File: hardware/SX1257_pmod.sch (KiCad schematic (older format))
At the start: 5 parts, among them J1 Conn_02x06_Odd_Even, U1 SX1257, Y1 32/36MHz ?ppm

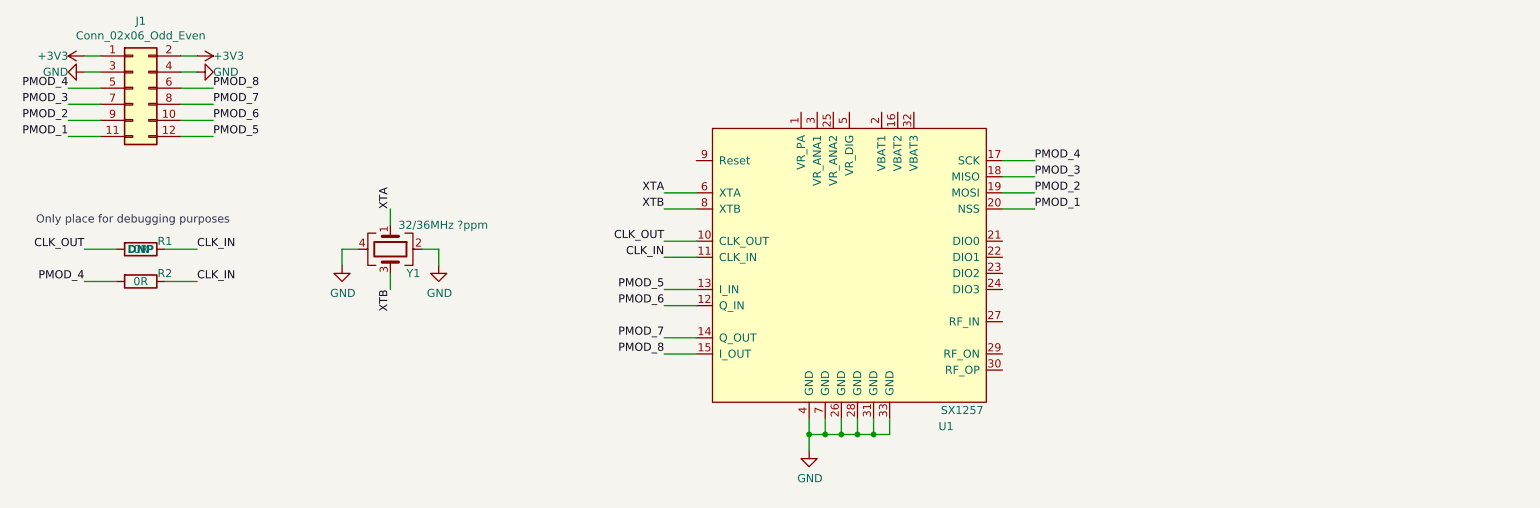
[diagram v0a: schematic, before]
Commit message: Added some caps etc
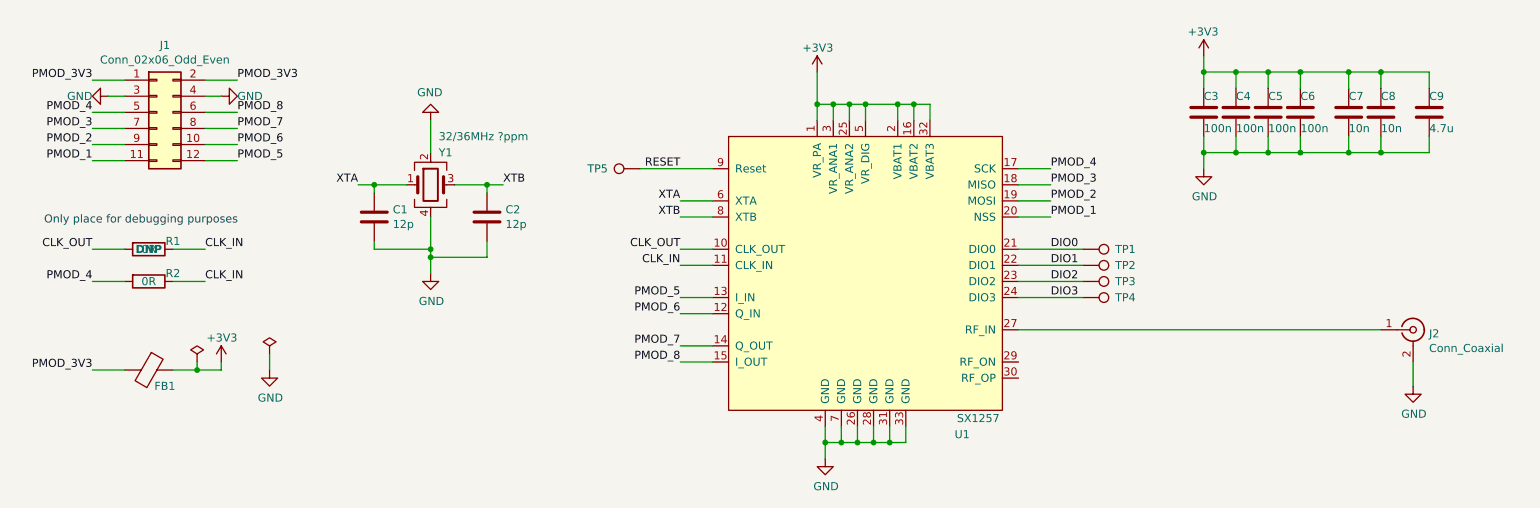
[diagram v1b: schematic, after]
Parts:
- added C1, C2: 12p, symbol Device:C
- added C3, C4, C5, C6: 100n, symbol Device:C
- added C7, C8: 10n, symbol Device:C
- added C9: 4.7u, symbol Device:C
- added FB1: Ferrite_Bead, symbol Device:Ferrite_Bead
- added J2: Conn_Coaxial, symbol Connector:Conn_Coaxial
- added TP1, TP2, TP3, TP4, TP5: TestPoint, symbol Connector:TestPoint
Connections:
- net +3V3: now also U1.1 (VR_PA), U1.16 (VBAT2), U1.2 (VBAT1), U1.25 (VR_ANA2), U1.3 (VR_ANA1), U1.32 (VBAT3), U1.5 (VR_DIG), C3.1, C4.1, C5.1, C6.1, C7.1, C8.1, C9.1, FB1.1; no longer J1.1 (Pin_1), J1.2 (Pin_2)
- net GND: now also C1.2, C2.2, C3.2, C4.2, C5.2, C6.2, C7.2, C8.2, C9.2, J2.2 (Ext)
- net XTA: now also C1.1
- net XTB: now also C2.1
- net DIO0: now reaches U1.21 (DIO0)
- net DIO0: now also TP1.1
- net DIO1: now reaches U1.22 (DIO1)
- net DIO1: now also TP2.1
- net DIO2: now reaches U1.23 (DIO2)
- net DIO2: now also TP3.1
- net DIO3: now reaches U1.24 (DIO3)
- net DIO3: now also TP4.1
- net at U1.27 (RF_IN): now also J2.1 (In)
- net RESET: now reaches U1.9 (Reset)
- net RESET: now also TP5.1
- new net PMOD_3V3: FB1.2, J1.1 (Pin_1), J1.2 (Pin_2)
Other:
- moved on the sheet: J1, R1, R2, U1, Y1

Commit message: Finalized the schematic
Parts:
- added AE1, AE2: PCB_Ant, symbol Device:Antenna
- added C10: 2.7p, symbol Device:C
- added C11, C12: 33p, symbol Device:C
- added C13, C16: 10p, symbol Device:C
- added C14: 3.3p, symbol Device:C
- added C15: 5.6p, symbol Device:C
- added C17, C18: 1u, symbol Device:C
- added C19: 10u, symbol Device:C
- added J3: SMA_F_TX, symbol Connector:Conn_Coaxial
- added L1: 15nH, symbol Device:L
- added L2: 10n, symbol Device:L
- added L3: 12n, symbol Device:L
- added R3, R4, R5, R6: 0R, symbol Device:R
- C1, C2: value 12p -> 16p
- C9: value 4.7u -> 1u
- J2: value Conn_Coaxial -> SMA_F_RX
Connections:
- net +3V3: now also C17.1, C18.1, C19.1
- net GND: now also C10.2, C12.2, C14.2, C15.2, C17.2, C18.2, C19.2, J3.2 (Ext), L3.2
- net at J2.1 (In): now also R4.1; no longer U1.27 (RF_IN)
- net RF_ON: now reaches U1.29 (RF_ON)
- net RF_ON: now also C11.2, C12.1
- net RF_OP: now reaches U1.30 (RF_OP)
- net RF_OP: now also C11.1, L2.1
- new net: C13.1, C15.1, L3.1, R3.2, R4.2
- new net: C13.2, L1.2
- new net: J3.1 (In), R6.1
- new net: C16.1, R5.2, R6.2
- new net: C14.1, C16.2, L2.2
- new net: AE2.1 (A), R5.1
- new net: AE1.1 (A), R3.1
- new net RF_IN: C10.1, L1.1, U1.27 (RF_IN)
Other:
- note added: "Check if 10mH or 10nH!"
- note added: "Not connected through the PMOD.\nRegisters are available through SPI."
- moved on the sheet: C1, C2, C3, C4, C5, C6, C7, C8, C9, TP1, TP2, TP3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

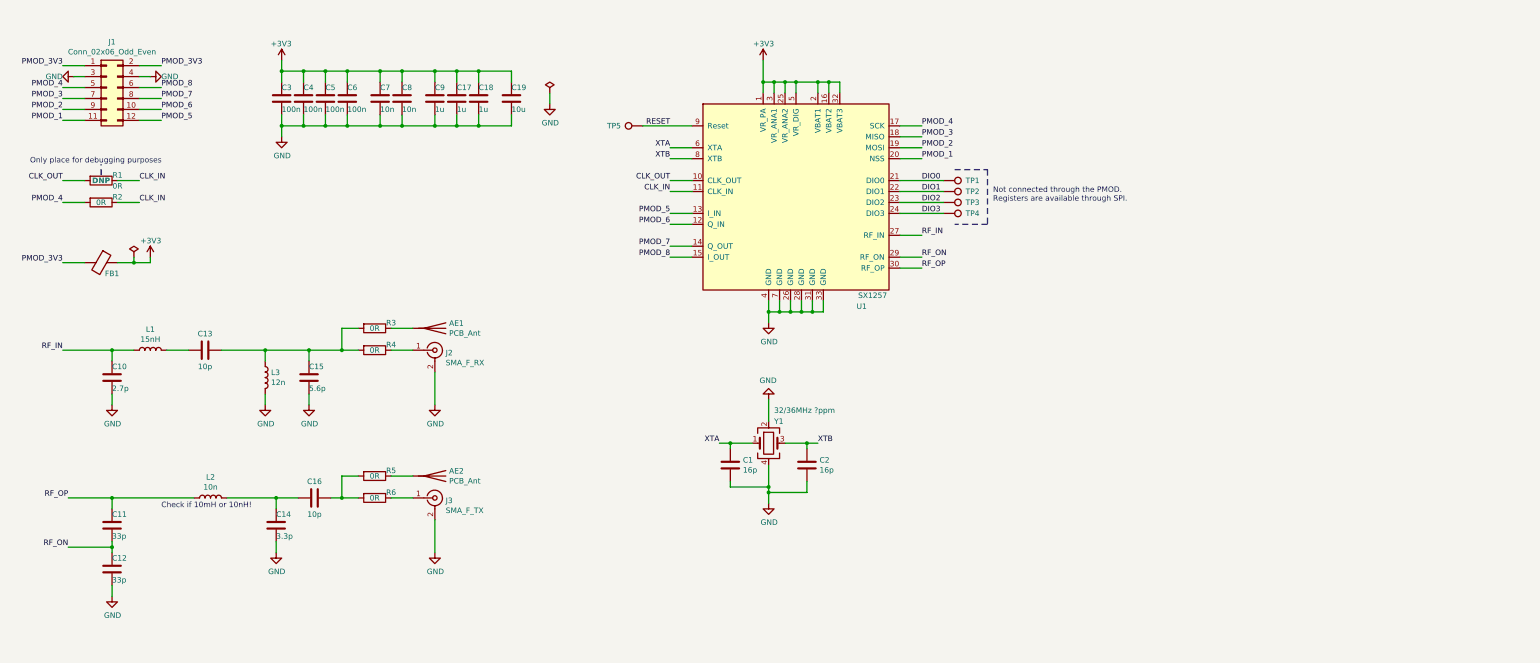
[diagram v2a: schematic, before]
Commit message: Remove CLK_OUT 0R and tidy up a bit.
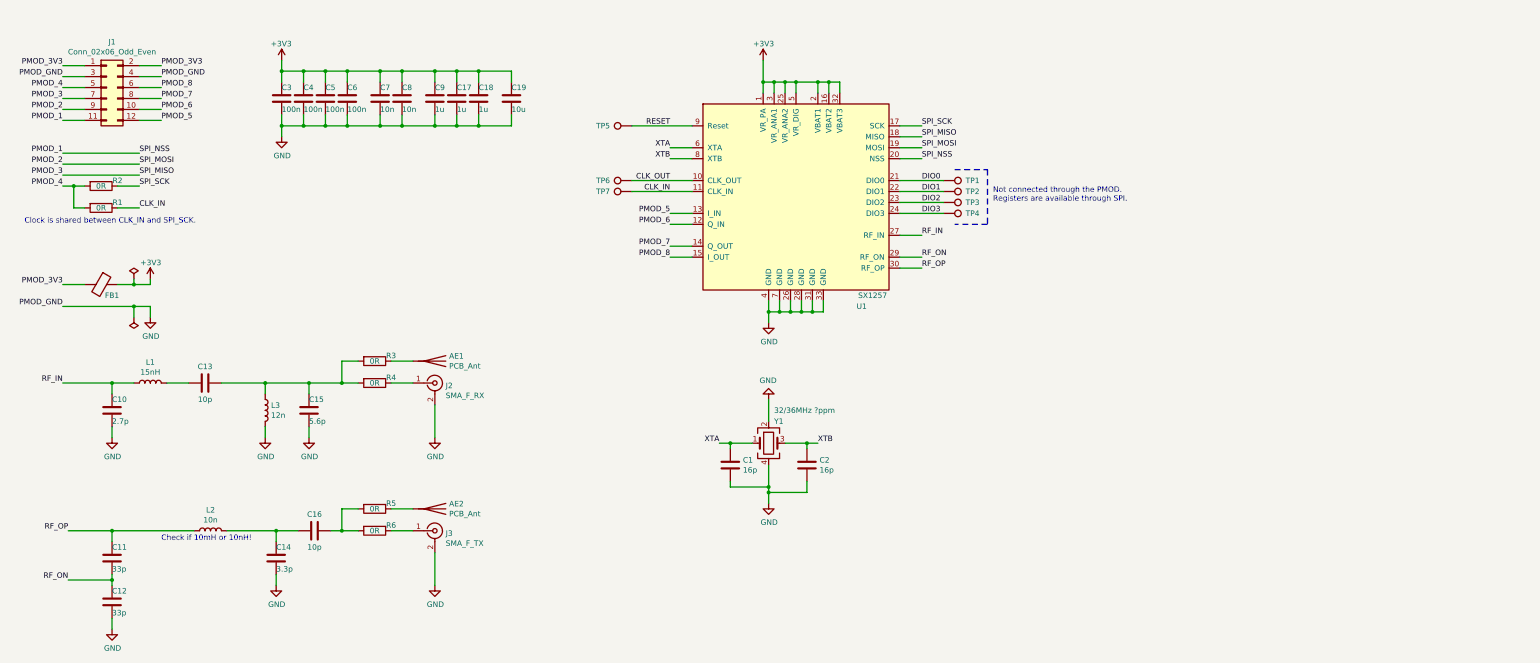
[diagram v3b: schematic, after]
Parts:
- added TP6, TP7: TestPoint, symbol Connector:TestPoint
- R1: Placement DNP -> (none)
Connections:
- net CLK_IN: now also TP7.1; no longer R2.1
- net CLK_OUT: now also TP6.1; no longer R1.2
- net PMOD_4: now also R1.2; no longer U1.17 (SCK)
- new net SPI_SCK: R2.1, U1.17 (SCK)
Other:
- note added: "Clock is shared between CLK_IN and SPI_SCK."
- note removed: "Only place for debugging purposes"
- moved on the sheet: AE1, AE2, C10, C11, C12, C13, C14, C15, C16, FB1, J2, J3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

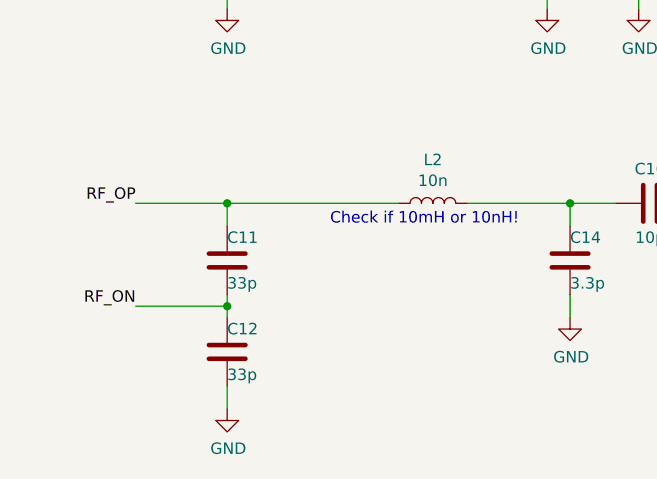
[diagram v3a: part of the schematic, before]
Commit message: Fix incorrect value of C11 33p => 3.3p
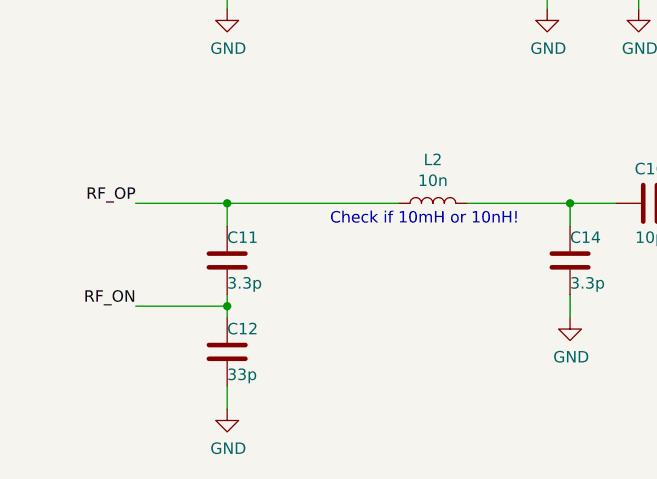
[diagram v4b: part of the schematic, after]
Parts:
- C11: value 33p -> 3.3p
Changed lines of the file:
@@
 P 1450 5550
 F 0 "C11" H 1450 5650 50  0000 L CNN
-F 1 "33p" H 1450 5450 50  0000 L CNN
+F 1 "3.3p" H 1450 5450 50  0000 L CNN
 F 2 "" H 1488 5400 50  0001 C CNN
 F 3 "~" H 1450 5550 50  0001 C CNN

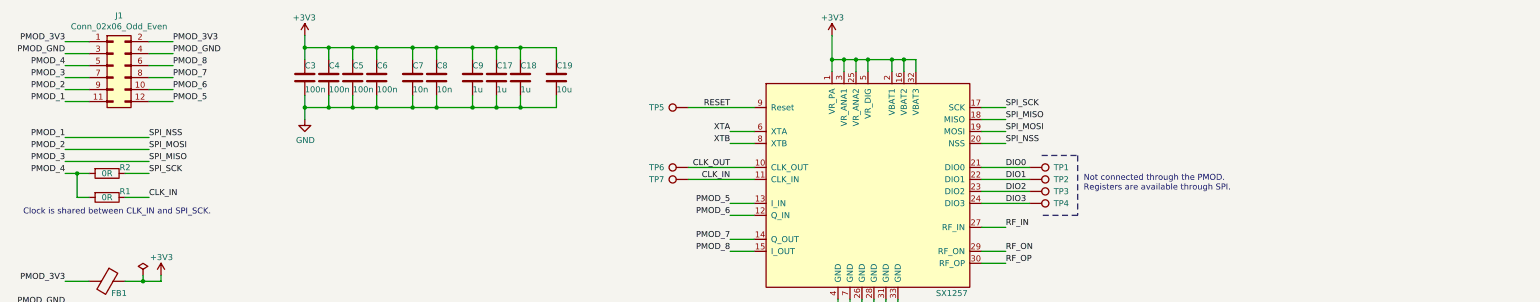
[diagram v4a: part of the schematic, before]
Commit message: Change clock
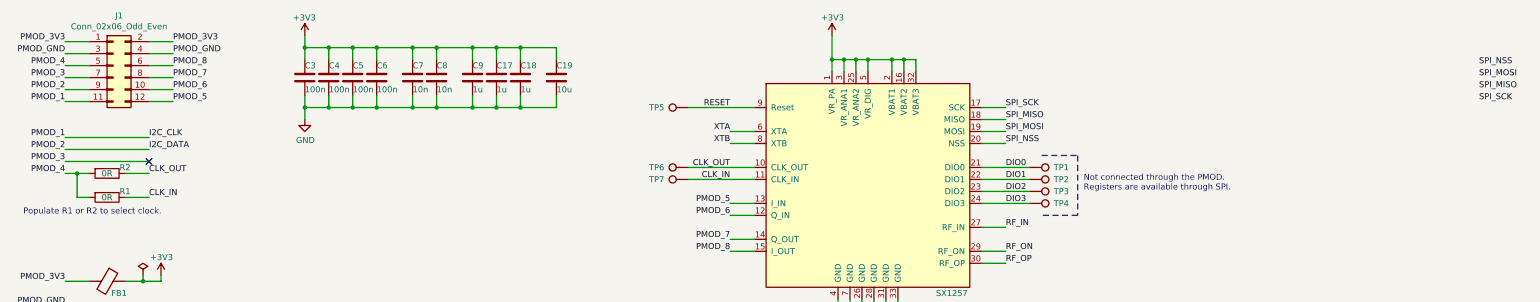
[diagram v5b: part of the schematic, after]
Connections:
- net CLK_OUT: now also R2.1
- net PMOD_3: no longer U1.18 (MISO)
- net SPI_SCK: no longer R2.1
- net PMOD_1 renamed I2C_CLK
- net I2C_CLK: no longer U1.20 (NSS)
- net PMOD_2 renamed I2C_DATA
- net I2C_DATA: no longer U1.19 (MOSI)
- new net SPI_MISO: U1.18 (MISO)
- new net SPI_MOSI: U1.19 (MOSI)
- new net SPI_NSS: U1.20 (NSS)
- no-connect marks 0 -> 1
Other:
- note added: "Populate R1 or R2 to select clock."
- note removed: "Clock is shared between CLK_IN and SPI_SCK."
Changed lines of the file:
@@
 EELAYER 26 0
 EELAYER END
-$Descr A4 11693 8268
+$Descr A3 16535 11693
 encoding utf-8
 Sheet 1 1
@@
 	1650 3250 1800 3250
 Text Notes 650  2500 0    50   ~ 0
-Clock is shared between CLK_IN and SPI_SCK.
+Populate R1 or R2 to select clock.
 $Comp
 L Connector:TestPoint TP6
@@
 Text Label 8850 1600 0    50   ~ 0
 SPI_SCK
-Text Label 1700 2150 0    50   ~ 0
+Text Label 12800 1550 0    50   ~ 0
 SPI_SCK
 $Comp
@@
 Text Label 8850 1900 0    50   ~ 0
 SPI_NSS
-Text Label 1700 2050 0    50   ~ 0
+Text Label 12800 1450 0    50   ~ 0
 SPI_MISO
+Text Label 12800 1350 0    50   ~ 0
+SPI_MOSI
+Text Label 12800 1250 0    50   ~ 0
+SPI_NSS
+Wire Wire Line
+	1000 2050 1700 2050
+Wire Wire Line
+	1000 1950 1700 1950
+Wire Wire Line
+	1000 1850 1700 1850
+Text Label 1700 2150 0    50   ~ 0
+CLK_OUT
+Text Label 1700 1850 0    50   ~ 0
+I2C_CLK
 Text Label 1700 1950 0    50   ~ 0
-SPI_MOSI
-Text Label 1700 1850 0    50   ~ 0
-SPI_NSS
-Wire Wire Line
-	1000 2050 1700 2050
-Wire Wire Line
-	1000 1950 1700 1950
-Wire Wire Line
-	1000 1850 1700 1850
+I2C_DATA
+NoConn ~ 1700 2050
 $EndSCHEMATC
